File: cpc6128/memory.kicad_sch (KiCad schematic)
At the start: 60 parts, among them IC103 AMS40025, IC104 74LS153, IC105 74LS153, IC109 74LS153, IC112 74LS32, IC113 74LS153, IC114 74LS373, IC115 74LS244, IC118 AMS40030, IC119 TMS4164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

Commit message: Update title blocks
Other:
- company: (none) -> Amstrad plc
- title: (none) -> CPC6128 MC0020x memory
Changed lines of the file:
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@@
 (kicad_sch (version 20211123) (generator eeschema)
   (paper "A3")
+  (title_block
+    (title "CPC6128 MC0020x memory")
+    (date "2022-08-20")
+    (rev "1")
+    (company "Amstrad plc")
+  )
   (junction (at 53.34 73.66) (diameter 0) (color 0 0 0 0)
   )

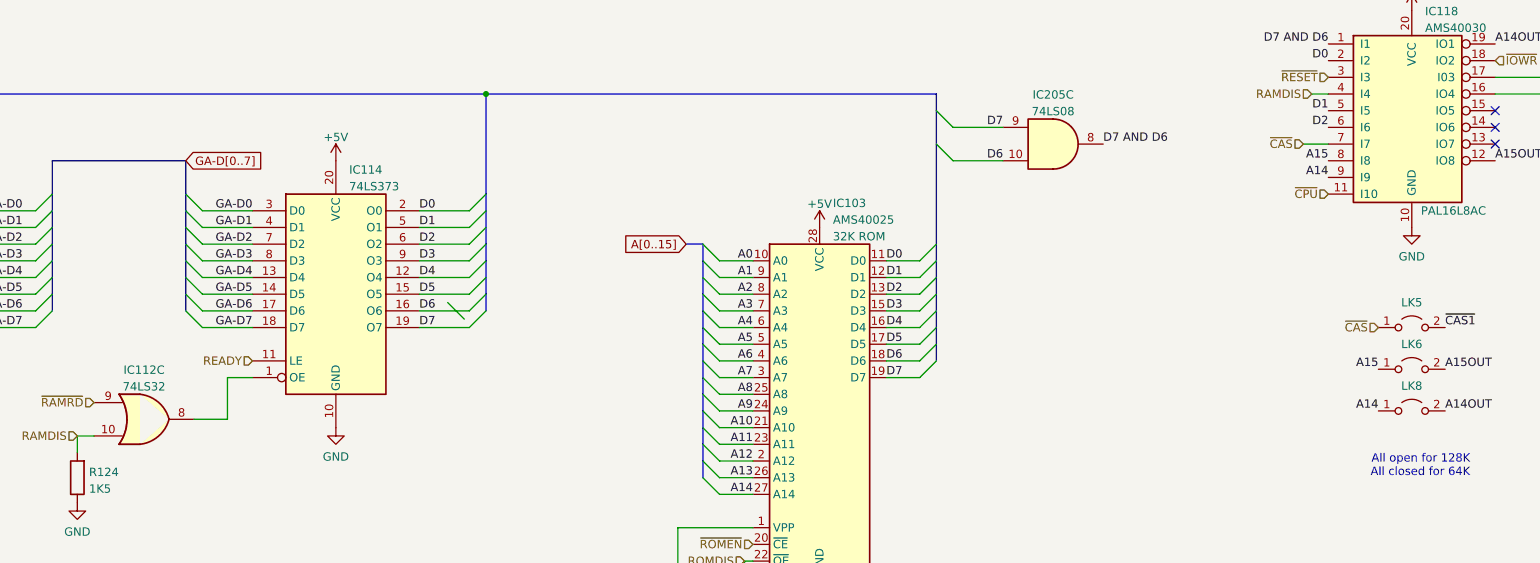
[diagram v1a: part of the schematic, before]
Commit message: Correct C136 (missing) and C314 (wrong footprint) Thanks @orzel!
Also migrated to KiCad 9.
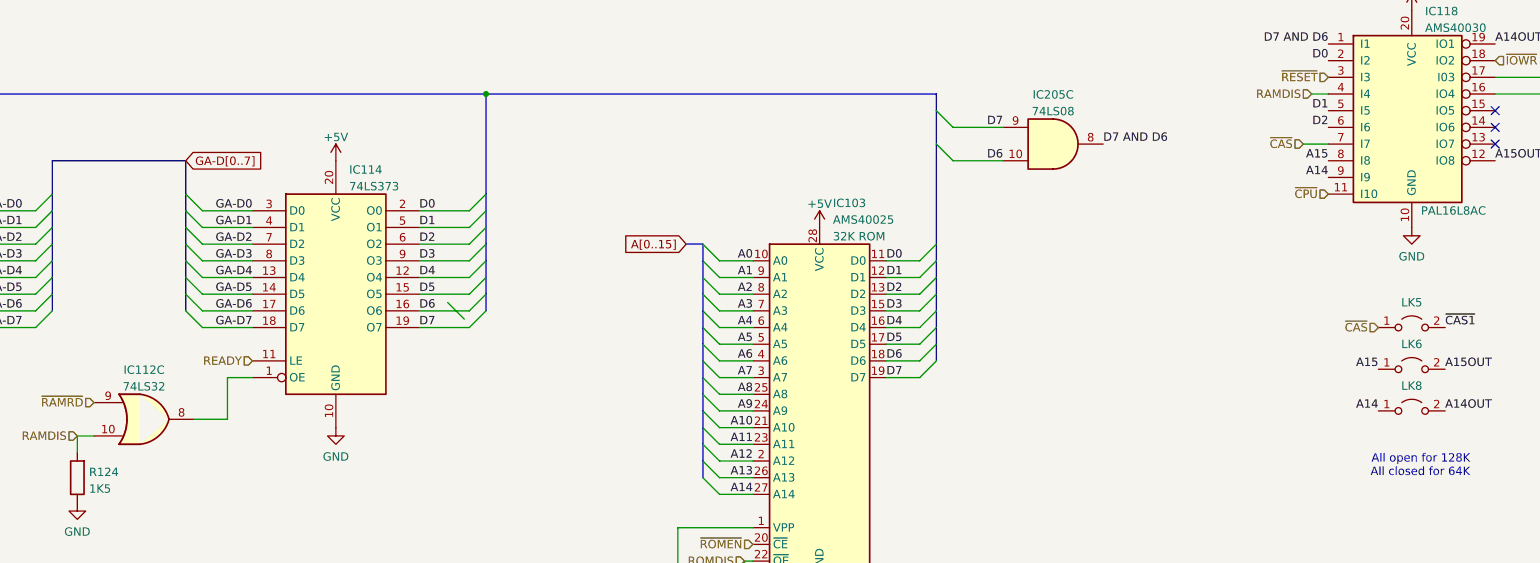
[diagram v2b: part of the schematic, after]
